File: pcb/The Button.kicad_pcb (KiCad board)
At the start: 2 copper layers, 54 x 74 mm, 28 parts, among them J1 Gnd, J2 2169890001, J3 Extra Pins, J4 Buttons, J5 Conn_01x05_Pin, SW8 SW_SPST BOOT, U1 LD1117S33TR_SOT223, U2 STM32C071KBTx, U5 USBLC6-2SC6

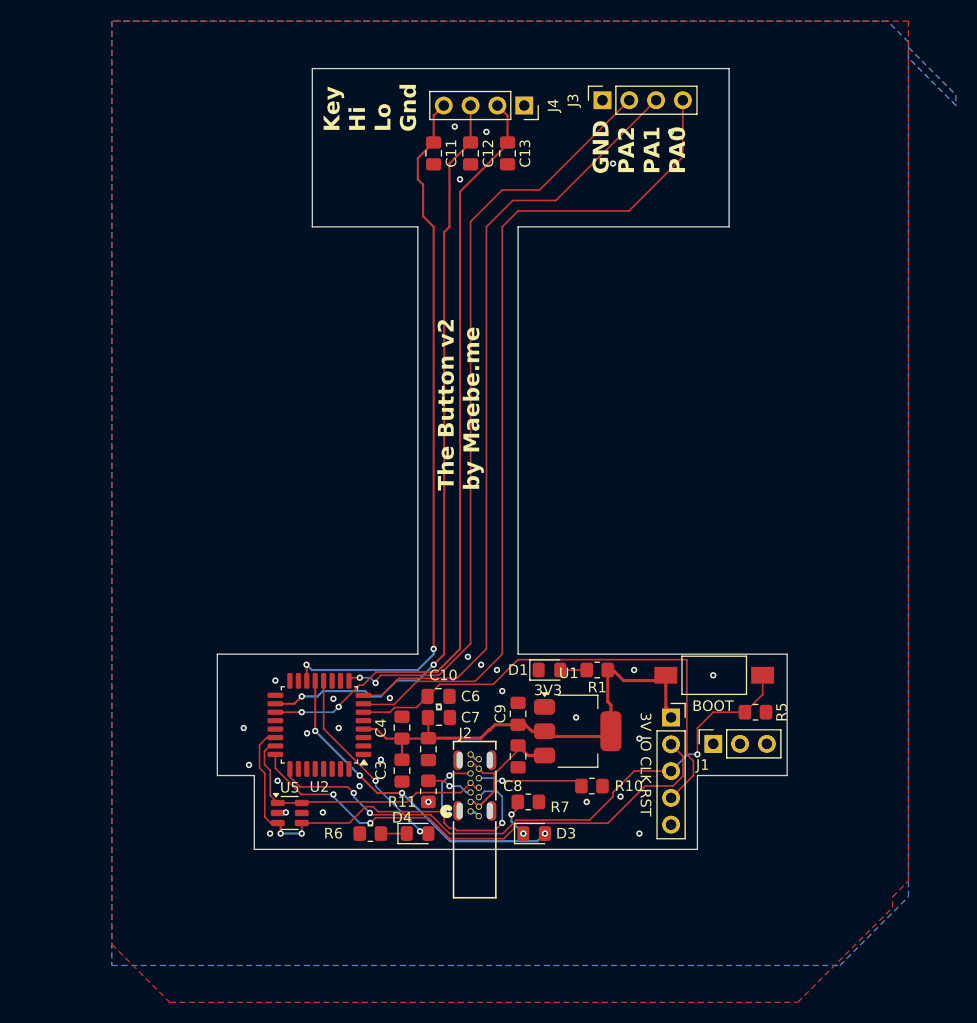
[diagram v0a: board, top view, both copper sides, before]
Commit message: Update pcb schematic to v3, layout pending
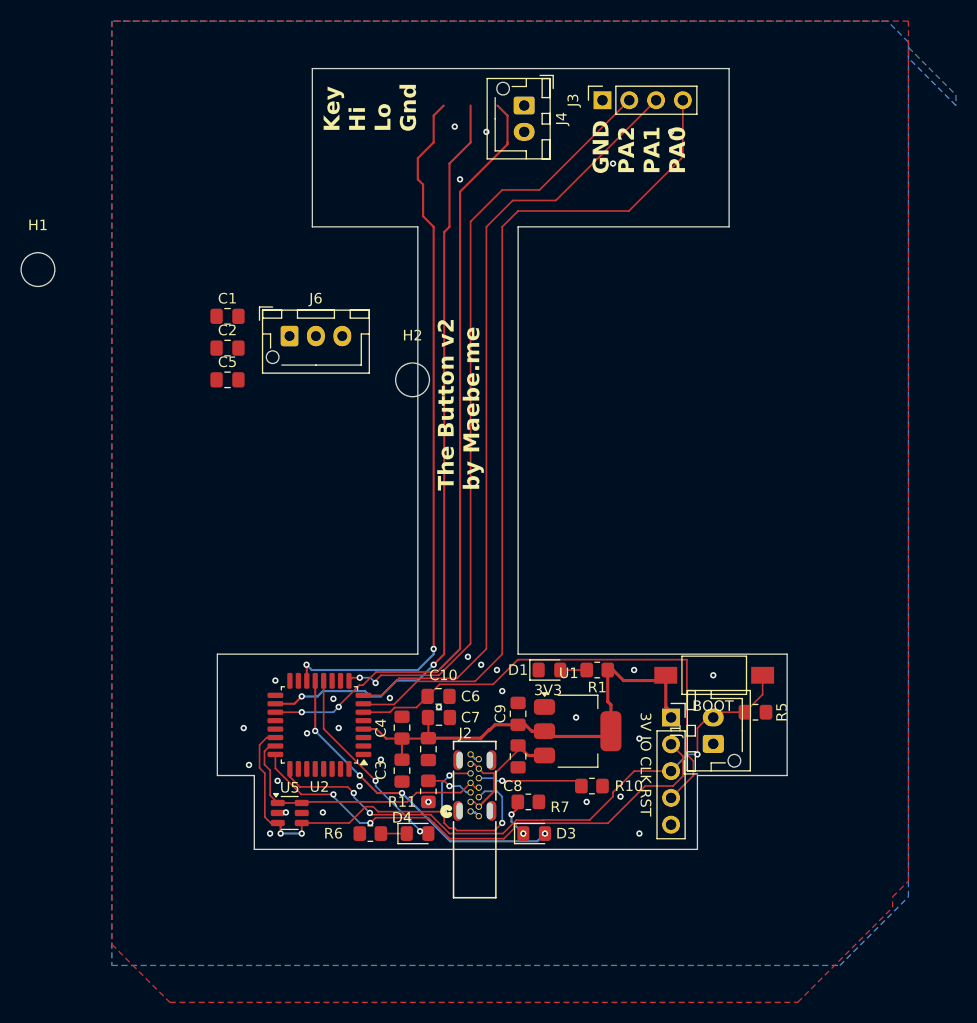
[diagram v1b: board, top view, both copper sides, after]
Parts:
- removed C11, C12, C13: 100nF, Capacitor_SMD:C_0805_2012Metric_Pad1.18x1.45mm_HandSolder
- added C1: 100nF, Capacitor_SMD:C_0805_2012Metric_Pad1.18x1.45mm_HandSolder, F.Cu at (147.5, 47.5)
- added C2: 100nF, Capacitor_SMD:C_0805_2012Metric_Pad1.18x1.45mm_HandSolder, F.Cu at (147.5, 50.5)
- added C5: 100nF, Capacitor_SMD:C_0805_2012Metric_Pad1.18x1.45mm_HandSolder, F.Cu at (147.5, 53.5)
- added H1: MountingHole, MountingHole:MountingHole_3.2mm_M3, F.Cu at (129.5, 43.0)
- added H2: MountingHole, MountingHole:MountingHole_3.2mm_M3, F.Cu at (165.0, 53.5)
- added J6: Conn_01x03, Connector_JST:JST_XH_B3B-XH-AM_1x03_P2.50mm_Vertical, F.Cu at (153.3, 49.4)
- J1: value Gnd -> Conn_01x02; footprint Connector_PinSocket_2.54mm:PinSocket_1x03_P2.54mm_Vertical -> Connector_JST:JST_XH_B2B-XH-AM_1x02_P2.50mm_Vertical
- J4: value Buttons -> Conn_01x02; footprint Connector_PinSocket_2.54mm:PinSocket_1x04_P2.54mm_Vertical -> Connector_JST:JST_XH_B2B-XH-AM_1x02_P2.50mm_Vertical
- R1: value 1K -> 5k
- R6, R7: value 5k -> 1k
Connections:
- J1 pad 1: GND -> BTN_HI
- J4 pad 1: GND -> BTN_LO
- J4 pad 2: /BTN_LO -> GND
- U2 pad 14: /BTN_KEY -> BTN_KEY
- U2 pad 18: /BTN_HI -> BTN_HI
- U2 pad 19: /BTN_LO -> BTN_LO
- U5 pad 5: unconnected-(U5-VBUS-Pad5) -> VDDA_5V
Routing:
- net BTN_LO: track 0.00 -> 73.8 mm, vias 0 -> 2
- net /BTN_LO: track 73.8 -> 0.00 mm, vias 2 -> 0
- net BTN_HI: track 0.00 -> 71.4 mm, vias 0 -> 2
- net /BTN_HI: track 71.4 -> 0.00 mm, vias 2 -> 0
- net BTN_KEY: track 0.00 -> 68.1 mm, vias 0 -> 2
- net /BTN_KEY: track 68.1 -> 0.00 mm, vias 2 -> 0

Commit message: Routing of pcb v3
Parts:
- removed J3: Extra Pins, Connector_PinSocket_2.54mm:PinSocket_1x04_P2.54mm_Vertical
- added J7: Conn_01x02, Connector_PinHeader_2.54mm:PinHeader_1x02_P2.54mm_Vertical, F.Cu at (162.0, 35.5)
- moved J1 61.9 mm to (170.0, 30.8)
- moved H1 57.0 mm to (154.0, 94.5)
- moved C5 46.1 mm to (190.5, 37.0)
- moved J6 39.9 mm to (189.5, 32.5), turned to 90 degrees
- moved C2 37.2 mm to (181.5, 35.5)
- moved R1 34.1 mm to (149.0, 87.5), turned to 90 degrees
- moved C6 31.5 mm to (198.0, 88.5), turned to 90 degrees
- moved C3 30.1 mm to (194.0, 88.5), turned to 90 degrees
- moved U2 29.3 mm to (185.0, 91.5)
- moved D1 29.1 mm to (149.0, 83.5), turned to -90 degrees
- moved C7 28.7 mm to (196.0, 88.5), turned to 90 degrees
- moved C4 28.1 mm to (192.0, 88.5)
- moved C1 26.9 mm to (171.5, 35.5)
- moved M3 26.5 mm to (160.0, 27.5)
- moved C10 25.6 mm to (193.0, 85.5)
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- renumbered H2 to M3
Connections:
- U2 pad 7: Net-(J3-Pin_4) -> unconnected-(U2-PA0-Pad7)
- U2 pad 8: Net-(J3-Pin_3) -> unconnected-(U2-PA1-Pad8)
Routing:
- net Net-(J3-Pin_4): track 80.9 -> 0.00 mm
- net Net-(J3-Pin_3): track 74.5 -> 0.00 mm
- net SWDIO: track 49.4 -> 14.6 mm, vias 2 -> 1
- net SWDCLK: track 57.0 -> 23.6 mm, vias 3 -> 2
- net VDD_3V: track 45.3 -> 76.2 mm, vias 0 -> 2
- net NRST: track 46.9 -> 25.3 mm
- net D_N: track 47.0 -> 26.5 mm, vias 5 -> 1
- net USR_LED_2: track 31.5 -> 13.5 mm, vias 4 -> 2
- net D_P: track 26.7 -> 11.5 mm
- net VDDA_5V: track 14.4 -> 26.6 mm, vias 0 -> 1
- net BTN_KEY: track 68.1 -> 77.4 mm, vias 2 -> 0
- net USR_LED_1: track 18.9 -> 28.0 mm
- net Net-(J2-CC2): track 10.0 -> 5.98 mm
- net BTN_HI: track 71.4 -> 68.5 mm
- net Net-(D3-K): track 3.79 -> 2.50 mm, vias 2 -> 0
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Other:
- board size 54 x 74 mm -> 54 x 76 mm
- board text added: "3v3"
- board text added: "4mm"
- board text added: "67mm"
- board text added: "6mm"
- board text added: "Hey, thanks for looking on this side :)"
- board text added: "M3"
- board text added: "The Button v3 by Maebe.me"
- board text removed: "3V3"
- board text removed: "GND PA2 PA1 PA0"
- board text removed: "Key Hi Lo Gnd"
- board text removed: "The Button v2 by Maebe.me"

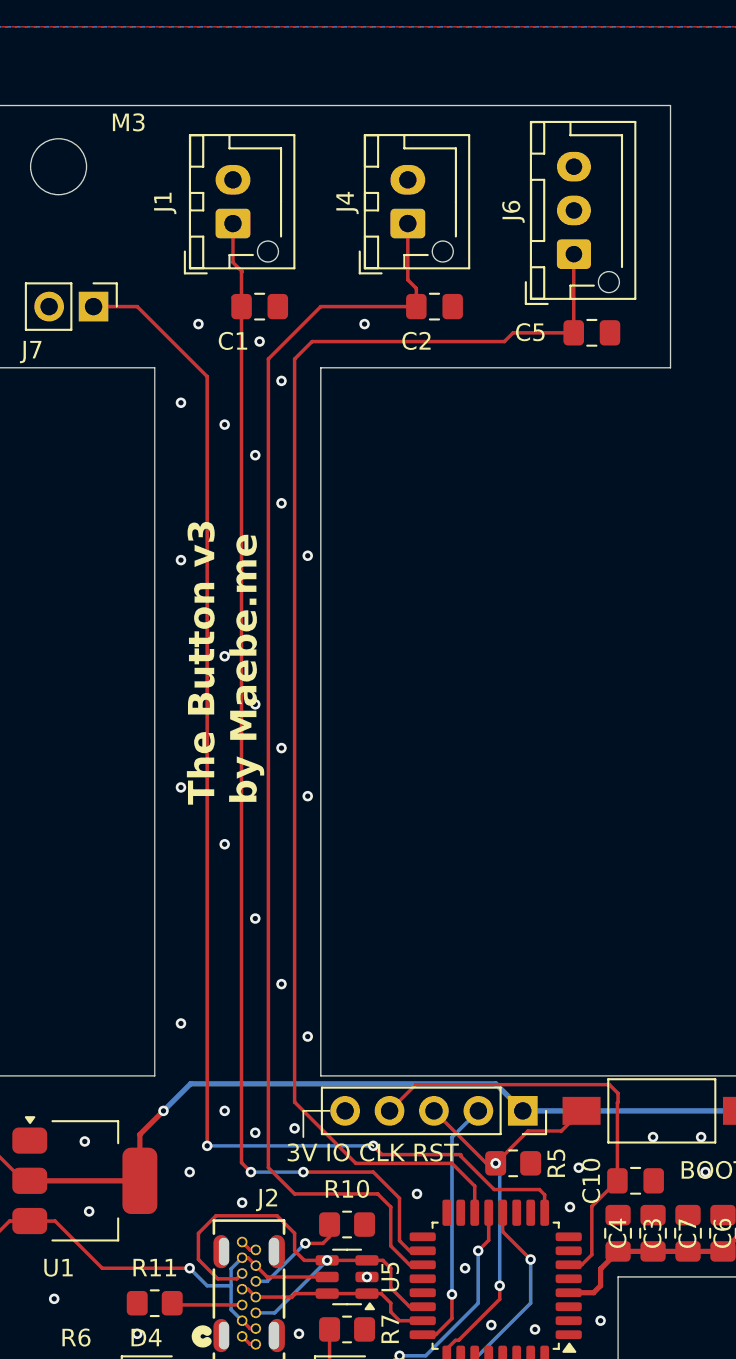
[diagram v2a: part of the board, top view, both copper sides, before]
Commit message: Added solder jumpers for hw config
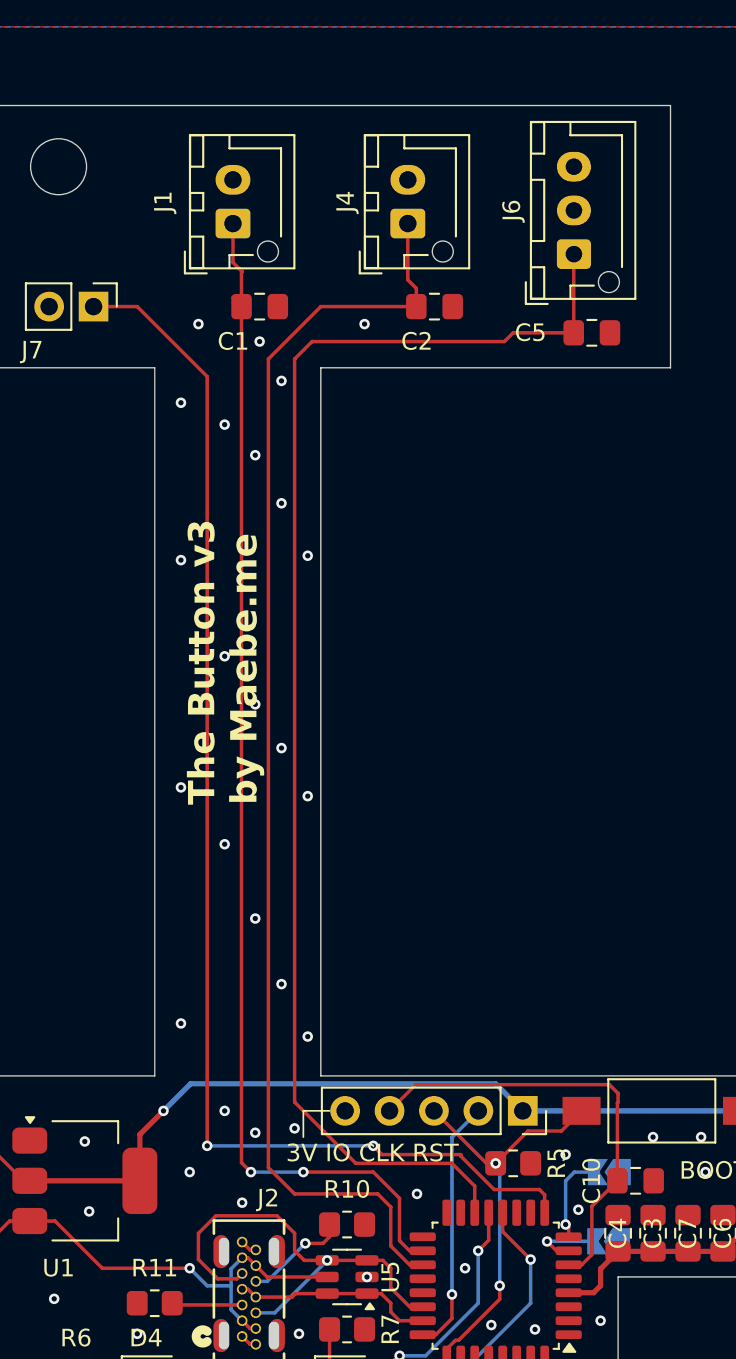
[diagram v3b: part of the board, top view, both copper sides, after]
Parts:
- removed M3: MountingHole, MountingHole:MountingHole_3.2mm_M3
- added H2: MountingHole, MountingHole:MountingHole_3.2mm_M3, F.Cu at (160.0, 27.5)
- added JP1: SolderJumper_2_Open, Jumper:SolderJumper-2_P1.3mm_Open_TrianglePad1.0x1.5mm, B.Cu at (191.5, 89.0)
- added JP2: SolderJumper_2_Open, Jumper:SolderJumper-2_P1.3mm_Open_TrianglePad1.0x1.5mm, B.Cu at (191.5, 85.0)
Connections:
- U2 pad 7: unconnected-(U2-PA0-Pad7) -> HW_CFG_1
- U2 pad 8: unconnected-(U2-PA1-Pad8) -> HW_CFG_2
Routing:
- net HW_CFG_2: track 0.00 -> 4.75 mm, vias 0 -> 1
- net HW_CFG_1: track 0.00 -> 4.28 mm, vias 0 -> 1

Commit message: Some minor tweaks, bump to v4
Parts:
- moved H1 0.50 mm to (154.0, 94.0)
- moved H2 0.50 mm to (160.0, 28.0)
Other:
- board text added: "66mm"
- board text added: "The Button v4 by Maebe.me"
- board text removed: "67mm"
- board text removed: "Hey, thanks for looking on this side :)"
- board text removed: "The Button v3 by Maebe.me"
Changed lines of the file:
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@@
 			(drillshape 0)
 			(scaleselection 1)
-			(outputdirectory "gerbers2/")
+			(outputdirectory "gerbersv4")
 		)
 	)
@@
 	)
 	(footprint "MountingHole:MountingHole_3.2mm_M3"
+		(locked yes)
 		(layer "F.Cu")
-		(at 160 27.5)
+		(at 160 28)
 		(descr "Mounting Hole 3.2mm, no annular, M3")
 		(tags "mounting hole 3.2mm no annular m3")
@@
 	)
 	(footprint "MountingHole:MountingHole_3.2mm_M3"
-		(locked yes)
 		(layer "F.Cu")
-		(at 154 94.5)
+		(at 154 94)
 		(descr "Mounting Hole 3.2mm, no annular, M3")
 		(tags "mounting hole 3.2mm no annular m3")
@@
 	)
 	(gr_line
-		(start 160 80.5)
-		(end 160 94.5)
-		(locked yes)
+		(start 160 80)
+		(end 160 94)
 		(stroke
 			(width 0.3)
@@
 	)
 	(gr_line
-		(start 154 94.5)
-		(end 160 94.5)
+		(start 154 94)
+		(end 160 94)
 		(stroke
 			(width 0.3)
@@
 	)
 	(gr_text "6mm\n"
-		(locked yes)
-		(at 164 97 0)
+		(at 158 86.5 90)
 		(layer "B.SilkS")
 		(effects
@@
 		)
 	)
-	(gr_text "67mm"
+	(gr_text "66mm"
 		(at 163.5 81 90)
 		(layer "B.SilkS")
@@
 	)
 	(gr_text "4mm"
-		(locked yes)
-		(at 150.5 87.5 -90)
+		(at 155.5 95 180)
 		(layer "B.SilkS")
 		(effects
@@
 		)
 	)
-	(gr_text "Hey, thanks for looking on this side :)"
-		(at 170 80.5 270)
+	(gr_text "4mm"
+		(at 153 80 90)
 		(layer "B.SilkS")
 		(effects
 			(font
-				(size 1.5 1.5)
+				(size 2 2)
 				(thickness 0.1)
 			)
@@
 		)
 	)
-	(gr_text "The Button v3\nby Maebe.me"
+	(gr_text "The Button v4\nby Maebe.me"
 		(at 171.5 64 90)
 		(layer "F.SilkS")
